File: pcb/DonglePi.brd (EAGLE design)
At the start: 83.5 x 17.8 mm, 10 parts, among them IC1 MCP1703DB

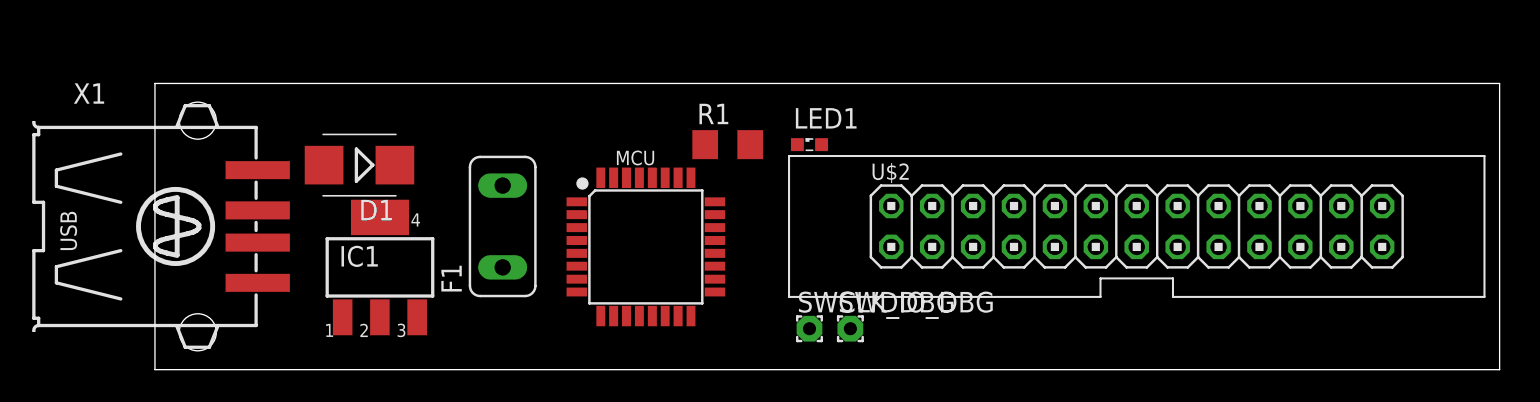
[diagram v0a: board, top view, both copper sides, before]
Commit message: Better components, noise protection.
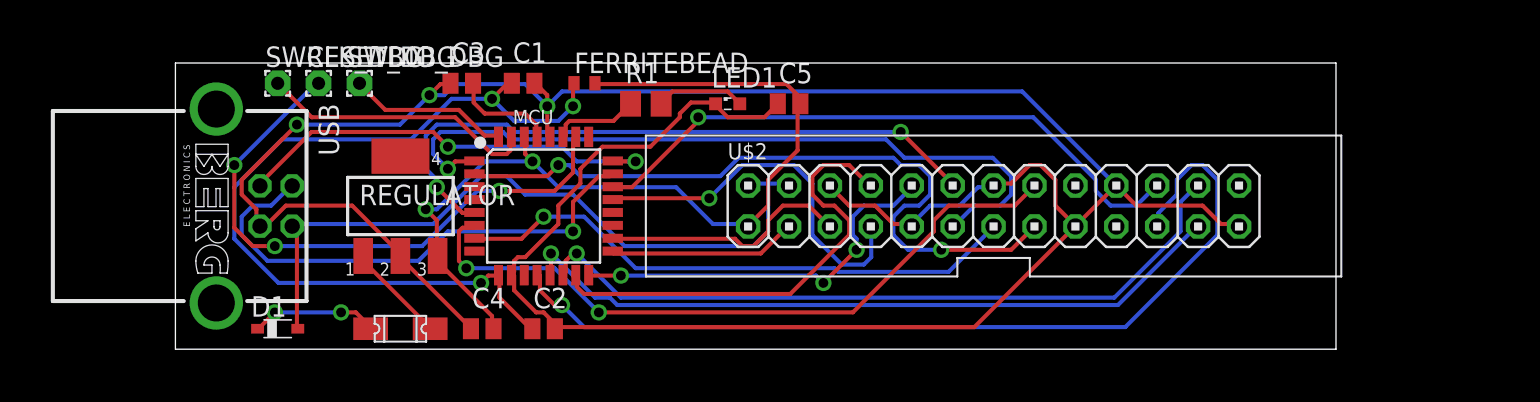
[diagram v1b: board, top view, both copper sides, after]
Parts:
- removed IC1: MCP1703DB, linear:SOT223
- removed X1: (no value), con-yamaichi:USB-A003
- added C1: 4.7uF, eagle-ltspice:C0504
- added C2, C4: 100nF, eagle-ltspice:C0504
- added C3, C5: 1uF, eagle-ltspice:C0504
- added FERRITEBEAD: BLM15HB121SN1, inductors:0402
- added REGULATOR: MCP1703DB, linear:SOT223
- added RESET_DBG: (no value), wirepad:1,6/0,8
- added USB: PN61729-S, con-berg:PN61729-S
- D1: value (none) -> BAT60J; device diode:SMB -> diode:SOD323_ST
- F1: value (none) -> 1206L; device fuse:TE5 -> gbin:1206L
- R1: device eagle-ltspice:R3216 -> rcl:M0805
- moved SWCLK_DBG 36.4 mm to (6.35, 16.5)
- moved SWDIO_DBG 34.1 mm to (11.4, 16.5)
- moved D1 11.4 mm to (6.35, 1.27), turned to 0 degrees
- moved U$2 8.98 mm to (50.8, 8.89)
- moved F1 8.98 mm to (14.0, 1.27), turned to 0 degrees
- moved MCU 6.84 mm to (22.9, 8.89)
- moved LED1 5.68 mm to (34.3, 15.2)
- moved R1 5.68 mm to (29.2, 15.2)
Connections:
- removed net VDDANA: MCU.9
- removed net VDDCORE: MCU.29
- removed net VDDIN: MCU.30
- new net N$3: MCU.27, R1.1
- new net N$6: C3.2, MCU.29
- new net N$7: MCU.26, RESET_DBG.1
- net +3V3: now also C4.2, C5.2, FERRITEBEAD.2, MCU.30, REGULATOR.3; no longer IC1.3
- net +5V: now also USB.1; no longer X1.1
- net GND: now also C1.2, C2.2, C3.1, C4.1, C5.1, REGULATOR.2, USB.4; no longer IC1.2, X1.4
- net N$1: now also F1.P$2, REGULATOR.1; no longer F1.2, IC1.1
- net N$2: now also F1.P$1; no longer F1.1
- net N$4: now also R1.2; no longer R1.1
- net N$5: now also C1.1, C2.1, FERRITEBEAD.1, MCU.9; no longer MCU.27, R1.2
- net PA24: now also USB.2; no longer X1.2
- net PA25: now also USB.3; no longer X1.3
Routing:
- net GND: track 0.00 -> 182.0 mm, vias 0 -> 3
- net PA09: track 0.00 -> 56.6 mm, vias 0 -> 1
- net +3V3: track 0.00 -> 56.3 mm, vias 0 -> 2
- net N$5: track 0.00 -> 52.5 mm, vias 0 -> 3
- net PA00: track 0.00 -> 46.9 mm, vias 0 -> 1
- net PA11: track 0.00 -> 45.5 mm, vias 0 -> 1
- net +5V: track 0.00 -> 45.2 mm
- net PA10: track 0.00 -> 44.9 mm, vias 0 -> 1
- net PA01: track 0.00 -> 44.7 mm, vias 0 -> 2
- net PA05: track 0.00 -> 43.7 mm, vias 0 -> 2
- net PA04: track 0.00 -> 41.1 mm, vias 0 -> 2
- net PA23: track 0.00 -> 38.9 mm, vias 0 -> 1
- net N$7: track 0.00 -> 36.9 mm, vias 0 -> 3
- net PA06: track 0.00 -> 35.4 mm, vias 0 -> 1
- net PA24: track 0.00 -> 32.1 mm, vias 0 -> 1
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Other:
- board size 83.5 x 17.8 mm -> 72.1 x 17.8 mm

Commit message: pass on sch
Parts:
- removed U$2: RPI_2X13, gbin:2X13
- removed USB: PN61729-S, con-berg:PN61729-S
- added LED2: _, eagle-ltspice:LED_SML0603
- added PA18_GPIO, PA19_GPIO, PA27_GPIO: _, wirepad:1,6/0,8
- added R2: 500, eagle-ltspice:R0201
- added RPIO: RPI_2X13, gbin:2X13
- added USB_MALE: USB-A-H, gbin:USB-A-H
- LED1, RESET_DBG, SWCLK_DBG, SWDIO_DBG: value (none) -> _
- R1: device rcl:M0805 -> eagle-ltspice:R0201
- moved RESET_DBG 61.0 mm to (68.1, 1.78)
- moved SWCLK_DBG 58.3 mm to (62.7, 1.78)
- moved SWDIO_DBG 55.9 mm to (65.4, 1.78)
- moved R1 39.4 mm to (68.6, 14.0)
- moved LED1 36.2 mm to (70.5, 15.2), turned to 270 degrees
- moved C5 10.2 mm to (27.9, 15.2), turned to 180 degrees
- moved C4 8.03 mm to (11.4, 3.81)
- moved C2 7.65 mm to (30.5, 1.91), turned to 90 degrees
- moved C3 4.58 mm to (15.2, 12.7), turned to 180 degrees
- moved C1 4.02 mm to (17.8, 15.2), turned to 180 degrees
- moved REGULATOR 3.71 mm to (10.3, 9.71)
- moved FERRITEBEAD 3.42 mm to (22.2, 15.2)
- moved F1 1.90 mm to (15.9, 1.27)
- moved D1 1.83 mm to (8.13, 1.71), turned to 180 degrees
- moved MCU 1.42 mm to (22.2, 7.62), turned to 45 degrees
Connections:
- new net N$6: LED2.A, R2.2
- net +3V3: now also RPIO.1; no longer U$2.1
- net +5V: now also RPIO.2, RPIO.4, USB_MALE.VBUS; no longer U$2.2, U$2.4, USB.1
- net GND: now also LED2.C, RPIO.14, RPIO.17, RPIO.20, RPIO.25, RPIO.6, RPIO.9, USB_MALE.GND; no longer U$2.14, U$2.17, U$2.20, U$2.25, U$2.6, U$2.9, USB.4
- net PA00: now also RPIO.11; no longer U$2.11
- net PA01: now also RPIO.15; no longer U$2.15
- net PA02: now also RPIO.26; no longer U$2.26
- net PA03: now also R2.1
- net PA04: now also RPIO.12; no longer U$2.12
- net PA05: now also RPIO.16; no longer U$2.16
- net PA06: now also RPIO.13; no longer U$2.13
- net PA07: now also RPIO.18; no longer U$2.18
- net PA08: now also RPIO.19; no longer U$2.19
- net PA09: now also RPIO.21; no longer U$2.21
- net PA10: now also RPIO.23; no longer U$2.23
- net PA11: now also RPIO.24; no longer U$2.24
- net PA14: now also RPIO.8; no longer U$2.8
- net PA15: now also RPIO.10; no longer U$2.10
- net PA16: now also RPIO.3; no longer U$2.3
- net PA17: now also RPIO.5; no longer U$2.5
- net PA18: now also PA18_GPIO.1
- net PA19: now also PA19_GPIO.1
- net PA22: now also RPIO.7; no longer U$2.7
- net PA23: now also RPIO.22; no longer U$2.22
- net PA24: now also USB_MALE.D-; no longer USB.2
- net PA25: now also USB_MALE.D+; no longer USB.3
- net PA27: now also PA27_GPIO.1
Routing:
- net GND: track 182.0 -> 0.00 mm, vias 3 -> 0
- net PA09: track 56.6 -> 0.00 mm, vias 1 -> 0
- net +3V3: track 56.3 -> 0.00 mm, vias 2 -> 0
- net N$5: track 52.5 -> 0.00 mm, vias 3 -> 0
- net PA00: track 46.9 -> 0.00 mm, vias 1 -> 0
- net PA11: track 45.5 -> 0.00 mm, vias 1 -> 0
- net +5V: track 45.2 -> 0.00 mm
- net PA10: track 44.9 -> 0.00 mm, vias 1 -> 0
- net PA01: track 44.7 -> 0.00 mm, vias 2 -> 0
- net PA05: track 43.7 -> 0.00 mm, vias 2 -> 0
- net PA04: track 41.1 -> 0.00 mm, vias 2 -> 0
- net PA23: track 38.9 -> 0.00 mm, vias 1 -> 0
- net N$7: track 36.9 -> 0.00 mm, vias 3 -> 0
- net PA06: track 35.4 -> 0.00 mm, vias 1 -> 0
- net PA24: track 32.1 -> 0.00 mm, vias 1 -> 0
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- added copper zone on layer 16, net GND
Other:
- board size 72.1 x 17.8 mm -> 72.7 x 18 mm

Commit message: silkscreen / routing POC
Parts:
- removed F1: 1206L, gbin:1206L
- removed PA18_GPIO, PA19_GPIO, PA27_GPIO: _, wirepad:1,6/0,8
- added FUSE: 1206L, gbin:1206L
- moved LED2 49.9 mm to (16.5, 8.89), turned to 0 degrees
- moved R2 44.7 mm to (19.1, 8.89), turned to 180 degrees
- moved LED1 42.5 mm to (27.9, 15.9)
- moved R1 41.9 mm to (26.7, 14.0), turned to 90 degrees
- moved SWCLK_DBG 16.2 mm to (69.7, 16.4)
- moved C2 15.9 mm to (14.6, 1.27)
- moved RESET_DBG 15.3 mm to (72.5, 16.4)
- moved C1 15.1 mm to (12.1, 1.27), turned to 90 degrees
- moved FERRITEBEAD 15.1 mm to (16.5, 1.27), turned to 90 degrees
- moved SWDIO_DBG 14.7 mm to (66.7, 16.4)
- moved C3 11.4 mm to (26.0, 16.5)
- moved C5 4.49 mm to (23.5, 15.9), turned to 270 degrees
- moved REGULATOR 3.42 mm to (11.6, 12.9)
- moved MCU 3.24 mm to (25.4, 8.26), turned to 0 degrees
- moved C4 2.84 mm to (12.7, 6.35)
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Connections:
- net N$1: now also FUSE.P$2; no longer F1.P$2
- net N$2: now also FUSE.P$1; no longer F1.P$1
- net PA18: no longer PA18_GPIO.1
- net PA19: no longer PA19_GPIO.1
- net PA27: no longer PA27_GPIO.1
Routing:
- net PA02: track 0.00 -> 74.2 mm, vias 0 -> 4
- net PA11: track 0.00 -> 62.4 mm
- net PA31: track 0.00 -> 55.8 mm, vias 0 -> 1
- net PA10: track 0.00 -> 54.1 mm, vias 0 -> 2
- net +5V: track 0.00 -> 51.1 mm, vias 0 -> 2
- net N$7: track 0.00 -> 50.9 mm
- net PA30: track 0.00 -> 50.2 mm, vias 0 -> 1
- net PA07: track 0.00 -> 49.2 mm, vias 0 -> 2
- net GND: track 0.00 -> 48.8 mm, vias 0 -> 3
- net +3V3: track 0.00 -> 48.3 mm, vias 0 -> 2
- net PA05: track 0.00 -> 47.6 mm, vias 0 -> 2
- net PA23: track 0.00 -> 45.3 mm
- net PA09: track 0.00 -> 44.2 mm, vias 0 -> 1
- net PA01: track 0.00 -> 42.5 mm, vias 0 -> 2
- net PA08: track 0.00 -> 40.9 mm, vias 0 -> 3
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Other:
- board size 72.7 x 18 mm -> 74 x 18.7 mm
- board text added: "DonglePI"
- board text added: "RST"
- board text added: "SWCLK"
- board text added: "SWDIO"
